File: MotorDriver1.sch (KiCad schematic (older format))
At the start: 38 parts, among them J18 43045-0802, J19 53426-0410, U37 MAX40056FAUA+, U38 DRV8312DDWR, U39 MAX40056FAUA+, U40 MIC2090-2YM5-TR

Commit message: PVT
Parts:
- C149: renamed from C157; footprint Capacitor-Chip:C_CHIP_1608_Reflow -> Capacitor-Chip:C_CHIP_1005_Hand_NoSilk; PartName GRM188R61E105KA12D -> TMK105BJ105MV-F
- C150: renamed from C158; PartName C1005X5R1V105K050BE -> TMK105BJ105MV-F
- C151: renamed from C159; PartName C1005X5R1V105K050BE -> TMK105BJ105MV-F
- C152: renamed from C160; footprint Capacitor-Chip:C_CHIP_1608_Reflow -> Capacitor-Chip:C_CHIP_1005_Hand_NoSilk; PartName GRM188R61E105KA12D -> TMK105BJ105MV-F
- C153: renamed from C161; footprint Capacitor-Chip:C_CHIP_1608_Reflow -> Capacitor-Chip:C_CHIP_1005_Hand_NoSilk; PartName GRM188R61E105KA12D -> TMK105BJ105MV-F
- C154: renamed from C162; footprint Capacitor-Chip:C_CHIP_1608_Reflow -> Capacitor-Chip:C_CHIP_1005_Hand_NoSilk; PartName GRM188R61E105KA12D -> TMK105BJ105MV-F
- C156: renamed from C164; PartName C1005X5R1V105K050BE -> TMK105BJ105MV-F
- C157: renamed from C165; PartName C1005X5R1V105K050BE -> TMK105BJ105MV-F
- C165: renamed from C173; PartName C1005X5R1V105K050BE -> TMK105BJ105MV-F
- R86: renamed from R101; value 2m -> 3m; PartName PMR18EZPJV2L0 -> PMR18EZPFV3L00
- R87: renamed from R102; value 2m -> 3m; PartName PMR18EZPJV2L0 -> PMR18EZPFV3L00
- renumbered C163 to C155, C166 to C158, C167 to C159, C168 to C160, C169 to C161, C170 to C162, C171 to C163, C172 to C164, L14 to L10, L15 to L11, L13 to L9, R97 to R82, R98 to R83, R99 to R84, R100 to R85, R103 to R88, R104 to R89, RA18 to RA19, RA19 to RA20, RA20 to RA21, U37 to U34, U38 to U35, U39 to U36, U40 to U37

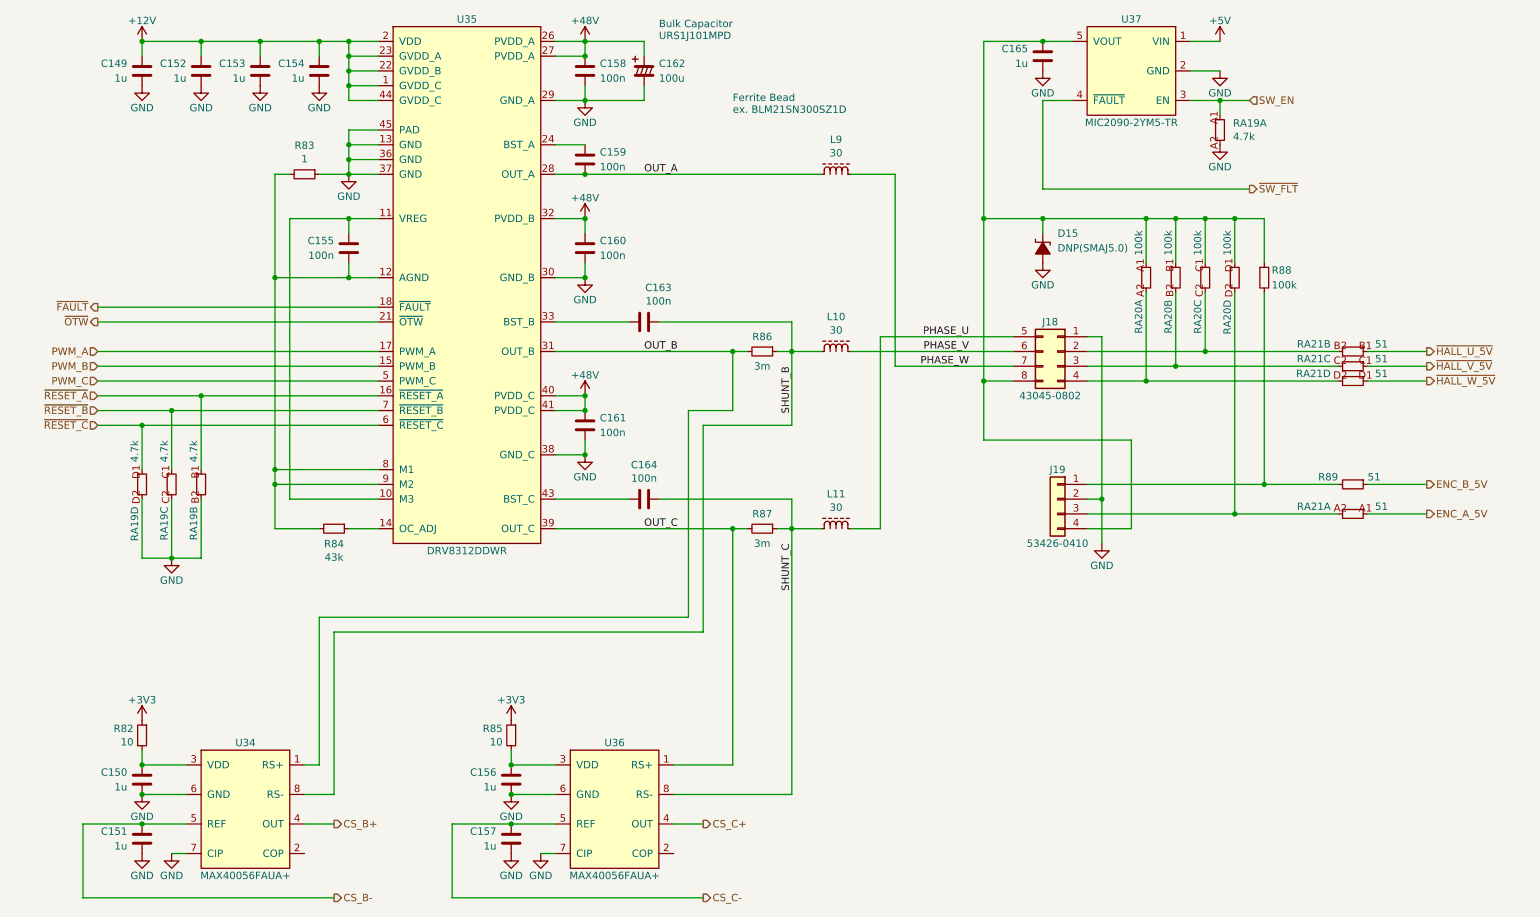
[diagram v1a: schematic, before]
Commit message: SBUにTVSダイオードを追加
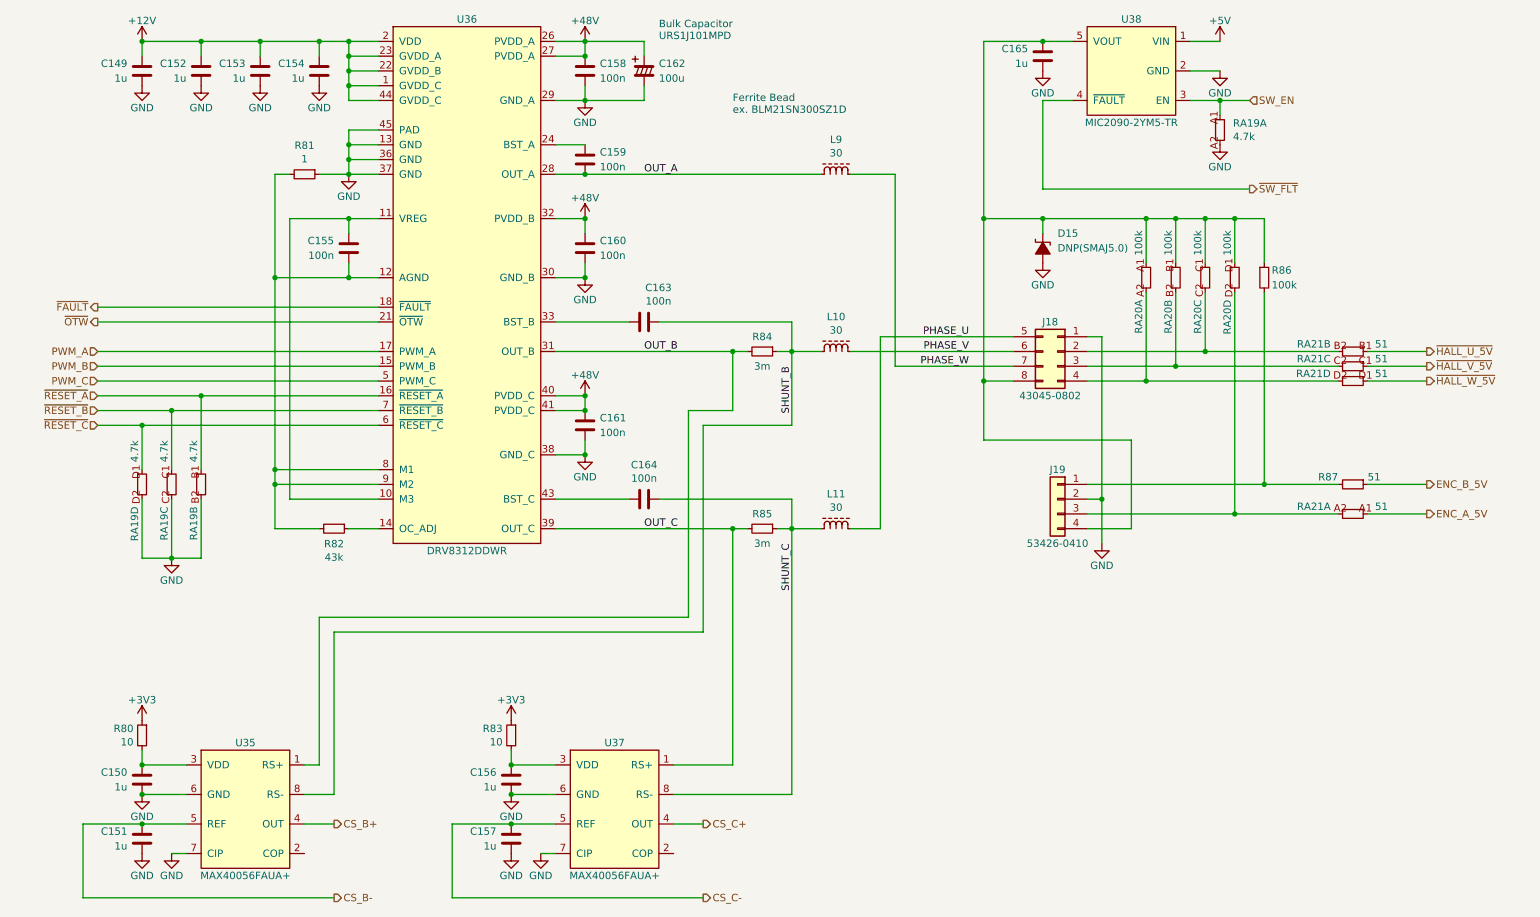
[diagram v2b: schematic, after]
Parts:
- renumbered R82 to R80, R83 to R81, R84 to R82, R85 to R83, R86 to R84, R87 to R85, R88 to R86, R89 to R87, U34 to U35, U35 to U36, U36 to U37, U37 to U38
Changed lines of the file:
@@
 AR Path="/5EFFEFDE/5F019185/5F01A02F" Ref="U?"  Part="1"
 AR Path="/5F062C46/5F01A02F" Ref="U?"  Part="1"
-AR Path="/5F235A43/5F01A02F" Ref="U35"  Part="1"
+AR Path="/5F235A43/5F01A02F" Ref="U36"  Part="1"
 AR Path="/5F237486/5F01A02F" Ref="U?"  Part="1"
-F 0 "U35" H 4000 4850 50  0000 C CNN
+F 0 "U36" H 4000 4850 50  0000 C CNN
 F 1 "DRV8312DDWR" H 4000 1250 50  0000 C CNN
 F 2 "IC-SOP:HTSSOP44-W6.1_EP4.31x8.26" H 4000 3000 50  0001 C CNN
@@
 AR Path="/5EFFEFDE/5F019185/5F03AF57" Ref="R?"  Part="1"
 AR Path="/5F062C46/5F03AF57" Ref="R?"  Part="1"
-AR Path="/5F235A43/5F03AF57" Ref="R83"  Part="1"
+AR Path="/5F235A43/5F03AF57" Ref="R81"  Part="1"
 AR Path="/5F237486/5F03AF57" Ref="R?"  Part="1"
-F 0 "R83" V 2705 2200 50  0000 C CNN
+F 0 "R81" V 2705 2200 50  0000 C CNN
 F 1 "1" V 2796 2200 50  0000 C CNN
 F 2 "Resistor-Chip:R_CHIP_1005_Hand_NoSilk" V 2950 2100 50  0001 C CNN
@@
 AR Path="/5EFFEFDE/5F019185/5F045450" Ref="R?"  Part="1"
 AR Path="/5F062C46/5F045450" Ref="R?"  Part="1"
-AR Path="/5F235A43/5F045450" Ref="R84"  Part="1"
+AR Path="/5F235A43/5F045450" Ref="R82"  Part="1"
 AR Path="/5F237486/5F045450" Ref="R?"  Part="1"
-F 0 "R84" V 3203 4600 50  0000 C CNN
+F 0 "R82" V 3203 4600 50  0000 C CNN
 F 1 "43k" V 3294 4600 50  0000 C CNN
 F 2 "Resistor-Chip:R_CHIP_1005_Hand_NoSilk" V 3150 4500 50  0001 C CNN
@@
 AR Path="/5EFFEFDE/5F019185/5F059CD1" Ref="R?"  Part="1"
 AR Path="/5F062C46/5F059CD1" Ref="R?"  Part="1"
-AR Path="/5F235A43/5F059CD1" Ref="R87"  Part="1"
+AR Path="/5F235A43/5F059CD1" Ref="R85"  Part="1"
 AR Path="/5F237486/5F059CD1" Ref="R?"  Part="1"
-F 0 "R87" V 5900 4600 50  0000 C CNN
+F 0 "R85" V 5900 4600 50  0000 C CNN
 F 1 "3m" V 6100 4600 50  0000 C CNN
 F 2 "Resistor-Chip:R_CHIP_3216_Reflow" V 6050 4500 50  0001 C CNN
@@
 P 2500 6500
 AR Path="/5F062C46/5F064C90" Ref="U?"  Part="1"
-AR Path="/5F235A43/5F064C90" Ref="U34"  Part="1"
+AR Path="/5F235A43/5F064C90" Ref="U35"  Part="1"
 AR Path="/5F237486/5F064C90" Ref="U?"  Part="1"
-F 0 "U34" H 2500 6950 50  0000 C CNN
+F 0 "U35" H 2500 6950 50  0000 C CNN
 F 1 "MAX40056FAUA+" H 2500 6050 50  0000 C CNN
 F 2 "IC-SOP:MSOP8" H 2500 6500 50  0001 C CNN
@@
 AR Path="/5EFFEFDE/5F019185/5F067792" Ref="R?"  Part="1"
 AR Path="/5F062C46/5F067792" Ref="R?"  Part="1"
-AR Path="/5F235A43/5F067792" Ref="R86"  Part="1"
+AR Path="/5F235A43/5F067792" Ref="R84"  Part="1"
 AR Path="/5F237486/5F067792" Ref="R?"  Part="1"
-F 0 "R86" V 5900 3400 50  0000 C CNN
+F 0 "R84" V 5900 3400 50  0000 C CNN
 F 1 "3m" V 6100 3400 50  0000 C CNN
 F 2 "Resistor-Chip:R_CHIP_3216_Reflow" V 6050 3300 50  0001 C CNN
@@
 P 5000 6500
 AR Path="/5F062C46/5F0A7FE5" Ref="U?"  Part="1"
-AR Path="/5F235A43/5F0A7FE5" Ref="U36"  Part="1"
+AR Path="/5F235A43/5F0A7FE5" Ref="U37"  Part="1"
 AR Path="/5F237486/5F0A7FE5" Ref="U?"  Part="1"
-F 0 "U36" H 5000 6950 50  0000 C CNN
+F 0 "U37" H 5000 6950 50  0000 C CNN
 F 1 "MAX40056FAUA+" H 5000 6050 50  0000 C CNN
 F 2 "IC-SOP:MSOP8" H 5000 6500 50  0001 C CNN
@@
 AR Path="/5EFFEFDE/5F019185/5F1AB60B" Ref="R?"  Part="1"
 AR Path="/5F062C46/5F1AB60B" Ref="R?"  Part="1"
-AR Path="/5F235A43/5F1AB60B" Ref="R82"  Part="1"
+AR Path="/5F235A43/5F1AB60B" Ref="R80"  Part="1"
 AR Path="/5F237486/5F1AB60B" Ref="R?"  Part="1"
-F 0 "R82" H 1858 6046 50  0000 L CNN
+F 0 "R80" H 1858 6046 50  0000 L CNN
 F 1 "10" H 1858 5955 50  0000 L CNN
 F 2 "Resistor-Chip:R_CHIP_1005_Hand_NoSilk" V 1850 5900 50  0001 C CNN
@@
 AR Path="/5EFFEFDE/5F019185/5E626021" Ref="R?"  Part="1"
 AR Path="/5F062C46/5E626021" Ref="R?"  Part="1"
-AR Path="/5F235A43/5E626021" Ref="R85"  Part="1"
+AR Path="/5F235A43/5E626021" Ref="R83"  Part="1"
 AR Path="/5F237486/5E626021" Ref="R?"  Part="1"
-F 0 "R85" H 4358 6046 50  0000 L CNN
+F 0 "R83" H 4358 6046 50  0000 L CNN
 F 1 "10" H 4358 5955 50  0000 L CNN
 F 2 "Resistor-Chip:R_CHIP_1005_Hand_NoSilk" V 4350 5900 50  0001 C CNN
@@
 AR Path="/5F5738E6/5EB01240" Ref="U?"  Part="1"
 AR Path="/5F235278/5EB01240" Ref="U?"  Part="1"
-AR Path="/5F235A43/5EB01240" Ref="U37"  Part="1"
-F 0 "U37" H 8500 1850 50  0000 C CNN
+AR Path="/5F235A43/5EB01240" Ref="U38"  Part="1"
+F 0 "U38" H 8500 1850 50  0000 C CNN
 F 1 "MIC2090-2YM5-TR" H 8500 1150 50  0000 C CNN
 F 2 "IC-SOT:SOT23-5" H 8500 1500 50  0001 C CNN
@@
 	10100 4500 10500 4500
 $Comp
-L passive:R R89
+L passive:R R87
 U 1 1 5E880D46
 P 10000 4300
-F 0 "R89" V 9950 4200 50  0000 R CNN
+F 0 "R87" V 9950 4200 50  0000 R CNN
 F 1 "51" V 9950 4400 50  0000 L CNN
 F 2 "Resistor-Chip:R_CHIP_1005_Hand_NoSilk" V 10050 4200 50  0001 C CNN
@@
 Connection ~ 9200 4500
 $Comp
-L passive:R R88
+L passive:R R86
 U 1 1 5E8D8A48
 P 9400 2900
-F 0 "R88" H 9450 2950 50  0000 L CNN
+F 0 "R86" H 9450 2950 50  0000 L CNN
 F 1 "100k" H 9450 2850 50  0000 L CNN
 F 2 "Resistor-Chip:R_CHIP_1005_Hand_NoSilk" V 9450 2800 50  0001 C CNN
